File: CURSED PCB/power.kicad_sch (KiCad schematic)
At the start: 16 parts, among them J4 Conn_01x04_Socket, U3 INA180A1, U4 SPX3819M5-L-3-3, U5 MCP1754S-3302xCB

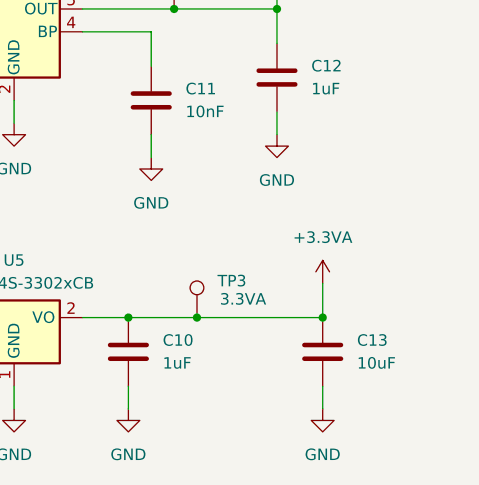
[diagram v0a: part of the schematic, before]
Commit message: Added reference voltage and some other stuff
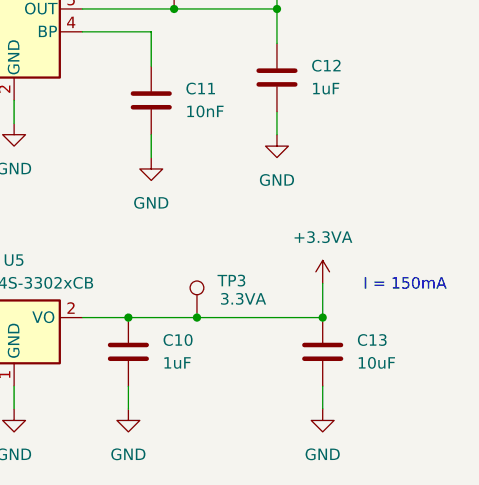
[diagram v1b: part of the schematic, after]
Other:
- note added: "I = 150mA"
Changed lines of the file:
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@@
 	(generator_version "9.0")
 	(paper "A4")
+	(text "I = 150mA "
+		(exclude_from_sim no)
+		(at 228.854 85.344 0)
+		(effects
+			(font
+				(size 1.27 1.27)
+			)
+		)
+	)
 	(text "Left to do on this page (nov-23)\n\nAdd decopuling capactiors, resistors amounts, use last year as reference"
 		(exclude_from_sim no)

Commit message: Changes to stuff
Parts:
- removed C7: 0.1uF, Capacitor_SMD:C_0201_0603Metric_Pad0.64x0.40mm_HandSolder, symbol PCM_Capacitor_US_AKL:C_0201
- removed TP1: 5V, TestPoint:TestPoint_Loop_D2.50mm_Drill1.0mm, symbol Connector:TestPoint
- removed U3: INA180A1, Package_TO_SOT_SMD:SOT-23-5, symbol Amplifier_Current:INA180A1
- added H1: MH1, MountingHole:MountingHole_2.2mm_M2_DIN965_Pad, symbol Mechanical:MountingHole_Pad
- added H2: MH2, MountingHole:MountingHole_2.2mm_M2_DIN965_Pad, symbol Mechanical:MountingHole_Pad
- added H3: MH3, MountingHole:MountingHole_2.2mm_M2_DIN965_Pad, symbol Mechanical:MountingHole_Pad
- added H4: MH4, MountingHole:MountingHole_2.2mm_M2_DIN965_Pad, symbol Mechanical:MountingHole_Pad
- F1: value 500mA Polyfuse -> Polyfuse
- R6: value 500m -> r
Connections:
- net GND: now also H1.1, H2.1, H3.1, H4.1
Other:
- moved on the sheet: R6

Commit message: fixed issue with mcu
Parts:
- added J?: Conn_01x02_Socket, symbol Connector:Conn_01x02_Socket
- added U2: INA180, Package_TO_SOT_SMD:SOT-23-5, symbol Amplifier_Current:INA180A1
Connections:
- net +5V: now also U2.3 (+)
- net GND: now also J?.1 (Pin_1), U2.2 (GND)
- net at F1.1, J4.4 (Pin_4): now also J?.2 (Pin_2)
- net at F1.2, R6.1: now also U2.4 (-)
- new net CUR_SENSE: U2.1
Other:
- moved on the sheet: F1, H1, H2, H3, H4, R6

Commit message: something something fixes to something related
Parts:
- removed J?: Conn_01x02_Socket, symbol Connector:Conn_01x02_Socket
- added J3: 691137710002, 691137710002:691137710002, symbol 691137710002:691137710002
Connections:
- net GND: now also J3.1
- net at F1.1, J4.4 (Pin_4): now also J3.2
- net +3.3V: now reaches U2.5 (V+)
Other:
- note removed: "I = 150mA"
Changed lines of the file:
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@@
 	(generator_version "9.0")
 	(paper "A4")
-	(text "I = 150mA "
-		(exclude_from_sim no)
-		(at 228.854 85.344 0)
-		(effects
-			(font
-				(size 1.27 1.27)
-			)
-		)
-	)
 	(text "Left to do on this page (nov-23)\n\nAdd decopuling capactiors, resistors amounts, use last year as reference"
 		(exclude_from_sim no)
@@
 		(pts
 			(xy 45.72 81.28) (xy 63.5 81.28)
+		)
+		(stroke
+			(width 0)
+			(type default)
+		)
+	)
+	(wire
+		(pts
+			(xy 95.25 49.53) (xy 95.25 67.31)
 		)
 		(stroke
@@
 	)
 	(symbol
+		(lib_id "691137710002:691137710002")
+		(at 40.64 78.74 90)
+		(unit 1)
+		(exclude_from_sim no)
+		(in_bom yes)
+		(on_board yes)
+		(dnp no)
+		(fields_autoplaced yes)
+		(property "Reference" "J3"
+			(at 41.91 72.39 90)
+			(effects
+				(font
+					(size 1.27 1.27)
+				)
+			)
+		)
+		(property "Value" "691137710002"
+			(at 41.91 74.93 90)
+			(effects
+				(font
+					(size 1.27 1.27)
+				)
+			)
+		)
+		(property "Footprint" "691137710002:691137710002"
+			(at 40.64 78.74 0)
+			(effects
+				(font
+					(size 1.27 1.27)
+				)
+				(justify bottom)
+				(hide yes)
+			)
+		)
+		(property "Datasheet" ""
+			(at 40.64 78.74 0)
+			(effects
+				(font
+					(size 1.27 1.27)
+				)
+				(hide yes)
+			)
+		)
+		(property "Description" ""
+			(at 40.64 78.74 0)
+			(effects
+				(font
+					(size 1.27 1.27)
+				)
+				(hide yes)
+			)
+		)
+		(property "DigiKey_Part_Number" "732-10955-ND"
+			(at 40.64 78.74 0)
+			(effects
+				(font
+					(size 1.27 1.27)
+				)
+				(justify bottom)
+				(hide yes)
+			)
+		)
+		(property "SnapEDA_Link" "https://www.snapeda.com/parts/691137710002/W%25C3%25BCrth+Elektronik+Midcom/view-part/?ref=snap"
+			(at 40.64 78.74 0)
+			(effects
+				(font
+					(size 1.27 1.27)
+				)
+				(justify bottom)
+				(hide yes)
+			)
+		)
+		(property "Description_1" "2 Position Wire to Board Terminal Block Horizontal with Board 0.197 (5.00mm) Through Hole"
+			(at 40.64 78.74 0)
+			(effects
+				(font
+					(size 1.27 1.27)
+				)
+				(justify bottom)
+				(hide yes)
+			)
+		)
+		(property "MF" "Würth Elektronik"
+			(at 40.64 78.74 0)
+			(effects
+				(font
+					(size 1.27 1.27)
+				)
+				(justify bottom)
+				(hide yes)
+			)
+		)
+		(property "Package" "None"
+			(at 40.64 78.74 0)
+			(effects
+				(font
+					(size 1.27 1.27)
+				)
+				(justify bottom)
+				(hide yes)
+			)
+		)
+		(property "Check_prices" "https://www.snapeda.com/parts/691137710002/W%25C3%25BCrth+Elektronik+Midcom/view-part/?ref=eda"
+			(at 40.64 78.74 0)
+			(effects
+				(font
+					(size 1.27 1.27)
+				)
+				(justify bottom)
+				(hide yes)
+			)
+		)
+		(property "MP" "691137710002"
+			(at 40.64 78.74 0)
+			(effects
+				(font
+					(size 1.27 1.27)
+				)
+				(justify bottom)
+				(hide yes)
+			)
+		)
+		(pin "2"
+		)
+		(pin "1"
+		)
+		(instances
+			(project ""
+				(path "/9fb1a86f-679c-4b88-9ed1-932f4f414580/78e664bb-f661-4ad0-951c-8ffe0c2483d0"
+					(reference "J3")
+					(unit 1)
+				)
+			)
+		)
+	)
+	(symbol
 		(lib_id "power:+3.3VA")
 		(at 219.71 85.09 0)
@@
 	)
 	(symbol
+		(lib_id "power:+3.3VA")
+		(at 95.25 49.53 0)
+		(unit 1)
+		(exclude_from_sim no)
+		(in_bom yes)
+		(on_board yes)
+		(dnp no)
+		(fields_autoplaced yes)
+		(property "Reference" "#PWR024"
+			(at 95.25 53.34 0)
+			(effects
+				(font
+					(size 1.27 1.27)
+				)
+				(hide yes)
+			)
+		)
+		(property "Value" "+3.3V"
+			(at 95.25 44.45 0)
+			(effects
+				(font
+					(size 1.27 1.27)
+				)
+			)
+		)
+		(property "Footprint" ""
+			(at 95.25 49.53 0)
+			(effects
+				(font
+					(size 1.27 1.27)
+				)
+				(hide yes)
+			)
+		)
+		(property "Datasheet" ""
+			(at 95.25 49.53 0)
+			(effects
+				(font
+					(size 1.27 1.27)
+				)
+				(hide yes)
+			)
+		)
+		(property "Description" "Power symbol creates a global label with name \"+3.3VA\""
+			(at 95.25 49.53 0)
+			(effects
+				(font
+					(size 1.27 1.27)
+				)
+				(hide yes)
+			)
+		)
+		(pin "1"
+		)
+		(instances
+			(project "sensor_1"
+				(path "/9fb1a86f-679c-4b88-9ed1-932f4f414580/78e664bb-f661-4ad0-951c-8ffe0c2483d0"
+					(reference "#PWR024")
+					(unit 1)
+				)
+			)
+		)
+	)
+	(symbol
 		(lib_id "power:GND")
 		(at 68.58 121.92 0)
@@
 					(unit 1)
 				)
-			)
-		)
-	)
-	(symbol
-		(lib_id "Connector:Conn_01x02_Socket")
-		(at 40.64 81.28 180)
-		(unit 1)
-		(exclude_from_sim no)
-		(in_bom yes)
-		(on_board yes)
-		(dnp no)
-		(fields_autoplaced yes)
-		(property "Reference" "J?"
-			(at 41.275 73.66 0)
-			(effects
-				(font
-					(size 1.27 1.27)
-				)
-			)
-		)
-		(property "Value" "Conn_01x02_Socket"
-			(at 41.275 76.2 0)
-			(effects
-				(font
-					(size 1.27 1.27)
-				)
-			)
-		)
-		(property "Footprint" ""
-			(at 40.64 81.28 0)
-			(effects
-				(font
-					(size 1.27 1.27)
-				)
-				(hide yes)
-			)
-		)
-		(property "Datasheet" "~"
-			(at 40.64 81.28 0)
-			(effects
-				(font
-					(size 1.27 1.27)
-				)
-				(hide yes)
-			)
-		)
-		(property "Description" "Generic connector, single row, 01x02, script generated"
-			(at 40.64 81.28 0)
-			(effects
-				(font
-					(size 1.27 1.27)
-				)
-				(hide yes)
-			)
-		)
-		(pin "2"
-		)
-		(pin "1"
-		)
-		(instances
-			(project ""
-				(path "/9fb1a86f-679c-4b88-9ed1-932f4f414580/78e664bb-f661-4ad0-951c-8ffe0c2483d0"
-					(reference "J?")
-					(unit 1)
-				)

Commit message: fixed errors
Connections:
- net CUR_SENSE renamed CUR_SEN
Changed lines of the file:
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@@
 	(wire
 		(pts
-			(xy 105.41 74.93) (xy 111.76 74.93)
+			(xy 105.41 74.93) (xy 114.3 74.93)
 		)
 		(stroke
@@
 		)
 	)
-	(hierarchical_label "CUR_SENSE"
-		(shape input)
-		(at 111.76 74.93 0)
+	(hierarchical_label "CUR_SEN"
+		(shape output)
+		(at 114.3 74.93 0)
 		(effects
 			(font

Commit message: something related to current and stuff
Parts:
- F1: value Polyfuse -> 170 mA
- R6: value r -> 194 m
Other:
- note removed: "Left to do on this page (nov-23) Add decopuling capactiors, resistors amounts, use last year as reference"
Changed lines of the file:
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@@
 	(generator_version "9.0")
 	(paper "A4")
-	(text "Left to do on this page (nov-23)\n\nAdd decopuling capactiors, resistors amounts, use last year as reference"
-		(exclude_from_sim no)
-		(at 13.97 95.758 0)
-		(effects
-			(font
-				(size 1.27 1.27)
-			)
-			(justify left)
-		)
-	)
 	(junction
 		(at 90.17 57.15)
@@
 			)
 		)
-		(property "Value" "Polyfuse"
+		(property "Value" "170 mA"
 			(at 69.85 53.34 90)
 			(effects
@@
 			)
 		)
-		(property "Value" "r"
+		(property "Value" "194 m"
 			(at 83.82 53.34 90)
 			(effects

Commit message: forgot to rename things
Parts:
- J3: value 691137710002 -> 2 Wire Block
- J4: value Conn_01x04_Socket -> CAN Bus Connector
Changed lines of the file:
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@@
 			)
 		)
-		(property "Value" "691137710002"
+		(property "Value" "2 Wire Block"
 			(at 41.91 74.93 90)
 			(effects
@@
 			)
 		)
-		(property "Value" "Conn_01x04_Socket"
+		(property "Value" "CAN Bus Connector"
 			(at 41.91 46.736 0)
 			(effects

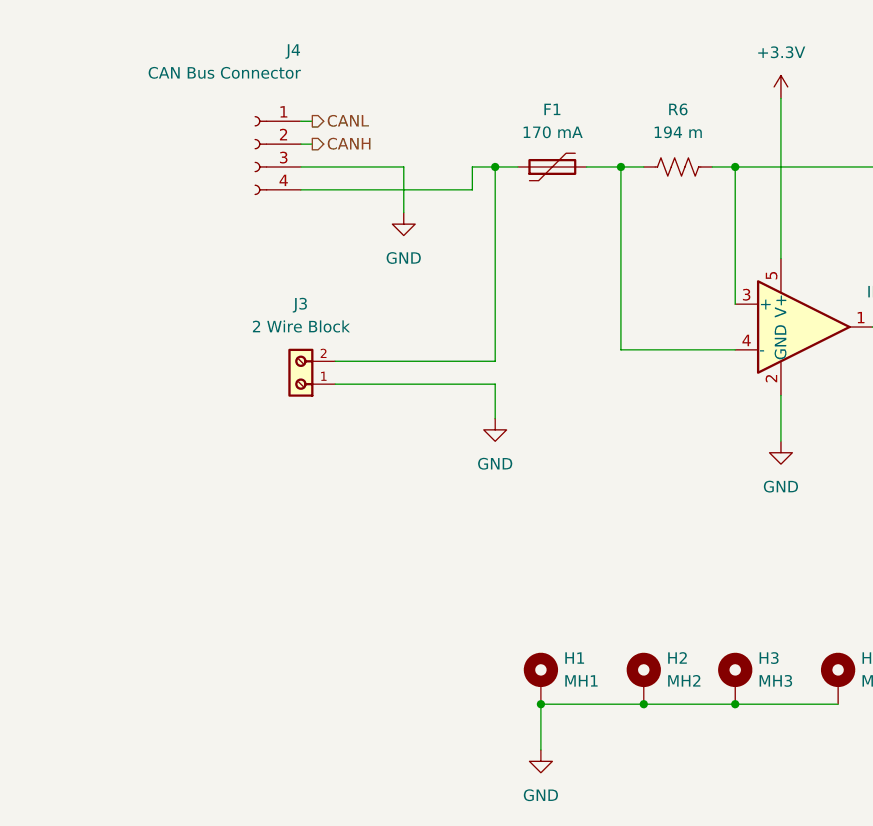
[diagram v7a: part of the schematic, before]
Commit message: some fixes to conner critique
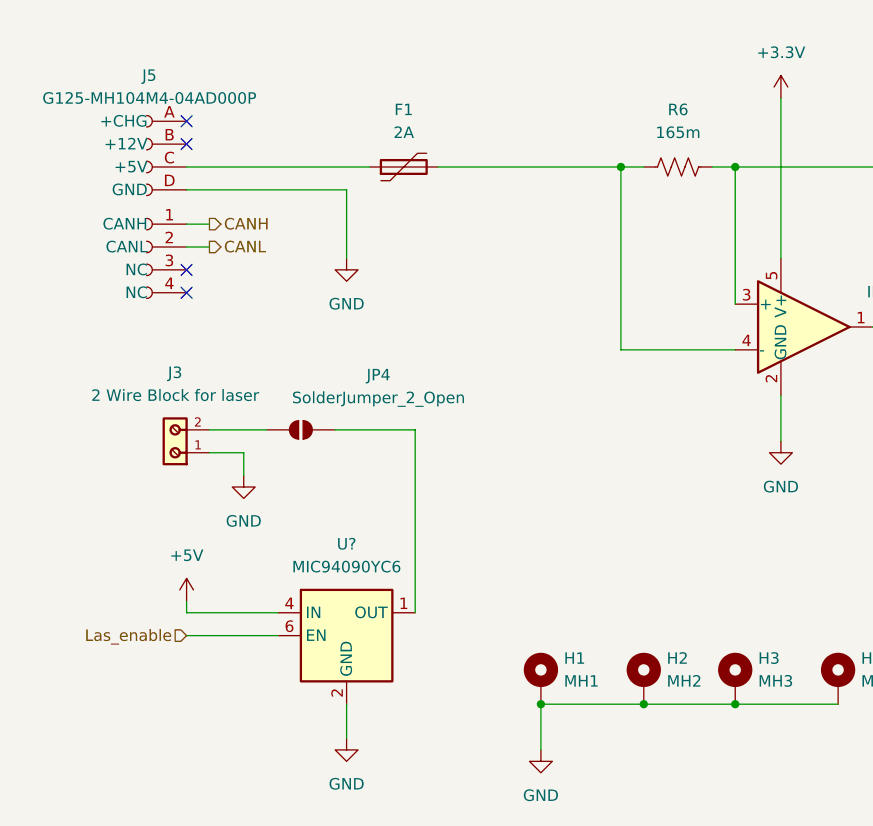
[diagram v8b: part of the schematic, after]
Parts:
- removed J4: CAN Bus Connector, canhw_footprints:PinSocket_4x2.54_SMD_90deg_952-3198-1-ND, symbol Connector:Conn_01x04_Socket
- added J5: G125-MH104M4-04AD000P, canhw_footprints:HARWIN_G125-MH104M4-04AD000P, symbol cashw:G125-MH104M4-04AD000P
- added JP4: SolderJumper_2_Open, Jumper:SolderJumper-2_P1.3mm_Open_Pad1.0x1.5mm, symbol Jumper:SolderJumper_2_Open
- added U?: MIC94090YC6, Package_TO_SOT_SMD:SOT-363_SC-70-6, symbol Power_Management:MIC94090YC6
- F1: value 170 mA -> 2A
- J3: value 2 Wire Block -> 2 Wire Block for laser
- R6: value 194 m -> 165m
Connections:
- net +5V: now also U?.4 (IN)
- net CANH: now also J5.1 (CANH)
- net CANL: now also J5.2 (CANL)
- net GND: now also J5.D (GND), U?.2 (GND), U?.5 (GND)
- net at J3.2: now also JP4.1 (A); no longer F1.1
- new net: F1.1, J5.C (+5V)
- new net: JP4.2 (B), U?.1 (OUT)
- new net Las_enable: U?.6 (EN)
- no-connect marks 0 -> 4
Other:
- moved on the sheet: F1, J3
